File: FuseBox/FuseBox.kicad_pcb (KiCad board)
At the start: 2 copper layers, 2 parts, among them J1 UJ31-CH-G2-SMT-TR, U1 TPS61040DBVR

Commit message: Changes
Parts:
- added D1: CUS10S40_H3F, Custom:CUS10S40H3F, F.Cu at (84.4, 74.7)
- added U2: LT3030EFE_TRPBF, Custom:LT8302ES8E_TRPBF, F.Cu at (77.4, 77.4)
- moved U1 52.1 mm to (84.3, 78.6)
- moved J1 48.2 mm to (80.1, 68.1)
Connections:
- J1 pad A1: unconnected-(J1-GND_1-PadA1) -> GND
- J1 pad A12: unconnected-(J1-GND_2-PadA12) -> GND
- J1 pad A4: unconnected-(J1-V_BUS_1-PadA4) -> VBUS
- J1 pad A5: unconnected-(J1-CC1-PadA5) -> Net-(J1-CC1)
- J1 pad A6: unconnected-(J1-DP1-PadA6) -> /USB_OTG_FS_DP
- J1 pad A7: unconnected-(J1-DN1-PadA7) -> /USB_OTG_FS_DN
- J1 pad A9: unconnected-(J1-V_BUS_2-PadA9) -> VBUS
- J1 pad B1: unconnected-(J1-GND_3-PadB1) -> GND
- J1 pad B12: unconnected-(J1-GND_4-PadB12) -> GND
- J1 pad B4: unconnected-(J1-VBUS_1-PadB4) -> VBUS
- J1 pad B5: unconnected-(J1-CC2-PadB5) -> Net-(J1-CC2)
- J1 pad B6: unconnected-(J1-DP2-PadB6) -> /USB_OTG_FS_DP
- J1 pad B7: unconnected-(J1-DN2-PadB7) -> /USB_OTG_FS_DN
- J1 pad B9: unconnected-(J1-VBUS_2-PadB9) -> VBUS
- J1 pad S1: unconnected-(J1-GND_5-PadS1) -> GND
- J1 pad S2: unconnected-(J1-GND_6-PadS2) -> GND
- J1 pad S3: unconnected-(J1-GND_7-PadS3) -> GND
- J1 pad S4: unconnected-(J1-GND_8-PadS4) -> GND
- U1 pad 1: unconnected-(U1-SW-Pad1) -> Net-(U1-SW)
- U1 pad 2: unconnected-(U1-GND-Pad2) -> GND
- U1 pad 3: unconnected-(U1-FB-Pad3) -> Net-(U1-FB)
- U1 pad 4: unconnected-(U1-EN-Pad4) -> +5V
- U1 pad 5: unconnected-(U1-VIN-Pad5) -> +5V

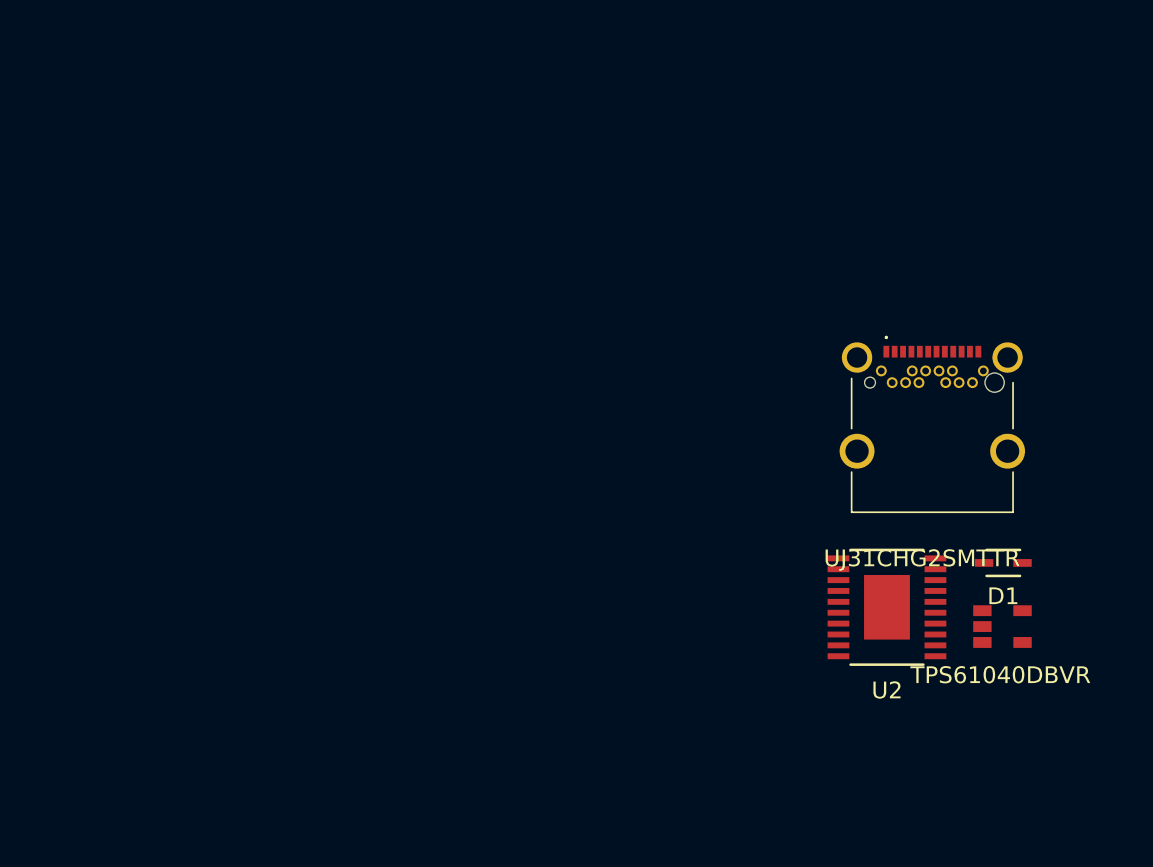
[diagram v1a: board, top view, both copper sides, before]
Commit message: Added STM32F4
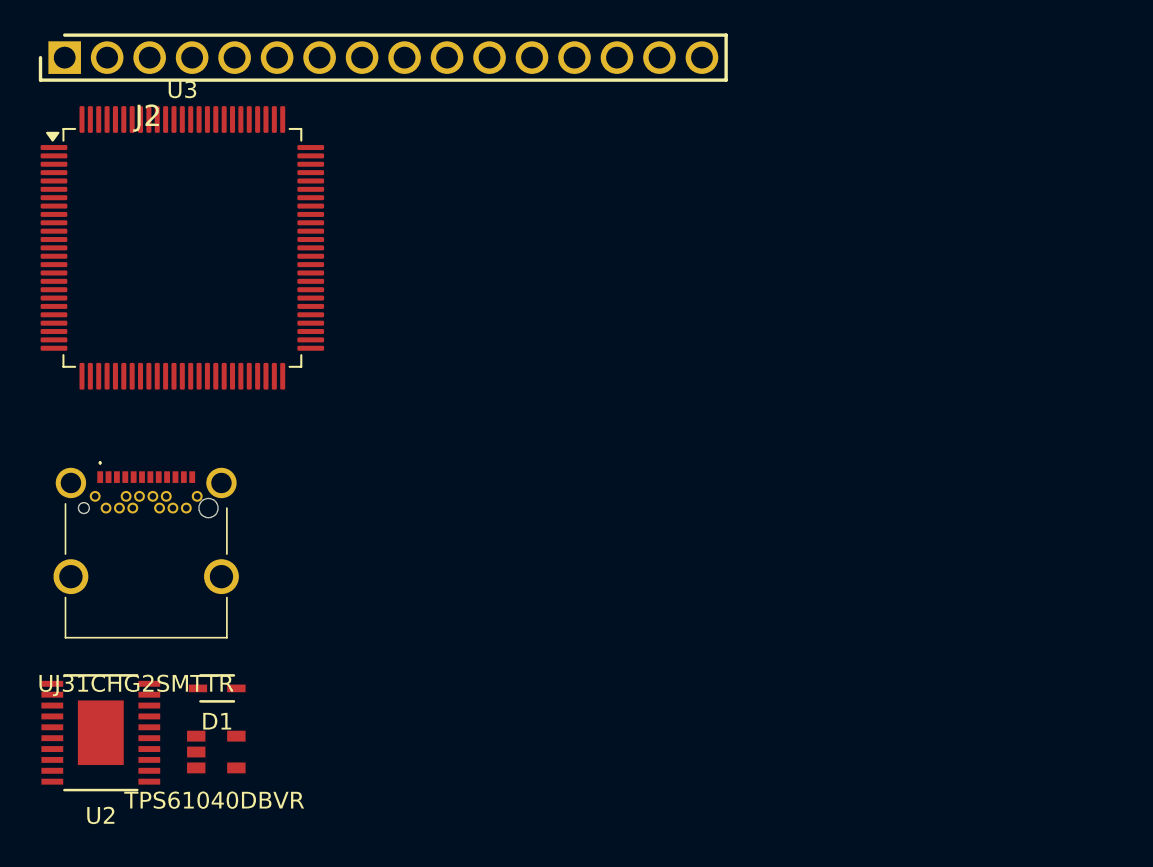
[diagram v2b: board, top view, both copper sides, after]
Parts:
- added J2: 61301611121, Custom:61301611121, F.Cu at (28.2, 44.5)
- added U3: STM32F407VGTx, Package_QFP:LQFP-100_14x14mm_P0.5mm, F.Cu at (35.3, 55.9)
- D1: value CUS10S40_H3F -> CUS10S40H3F
- J1: value UJ31-CH-G2-SMT-TR -> UJ31CHG2SMTTR
- U2: value LT3030EFE_TRPBF -> LT3030EFETRPBF; footprint Custom:LT8302ES8E_TRPBF -> Custom:LT8302ES8ETRPBF
- moved J1 47.6 mm to (33.1, 75.6)
- moved U2 47.6 mm to (30.4, 84.9)
- moved U1 47.6 mm to (37.3, 86.1)
- moved D1 47.6 mm to (37.4, 82.2)
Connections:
- net +12V4 renamed VCC_12V
